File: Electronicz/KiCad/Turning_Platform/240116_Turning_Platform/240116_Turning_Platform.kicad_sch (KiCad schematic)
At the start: 5 parts, among them J1 Display, J2 +12V, J3 GND, J4 Conn_01x05_Pin

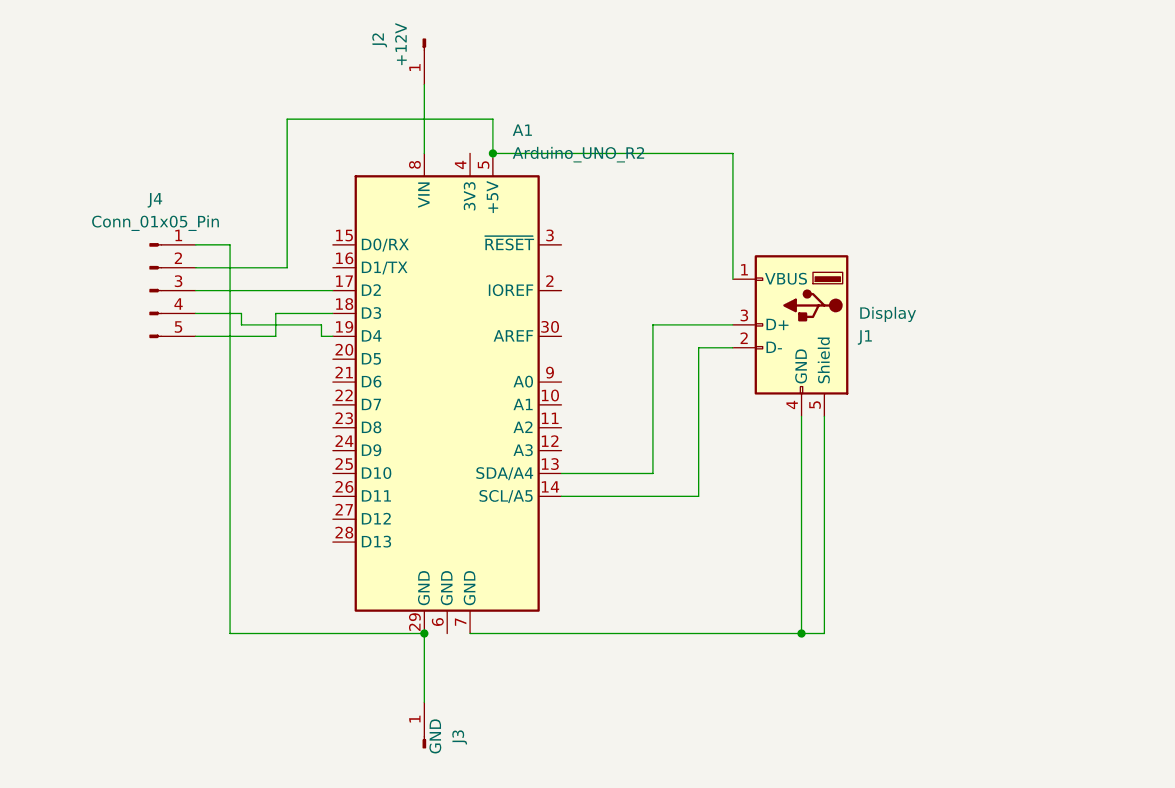
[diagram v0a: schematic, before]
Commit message: Make Turning Plate PCB
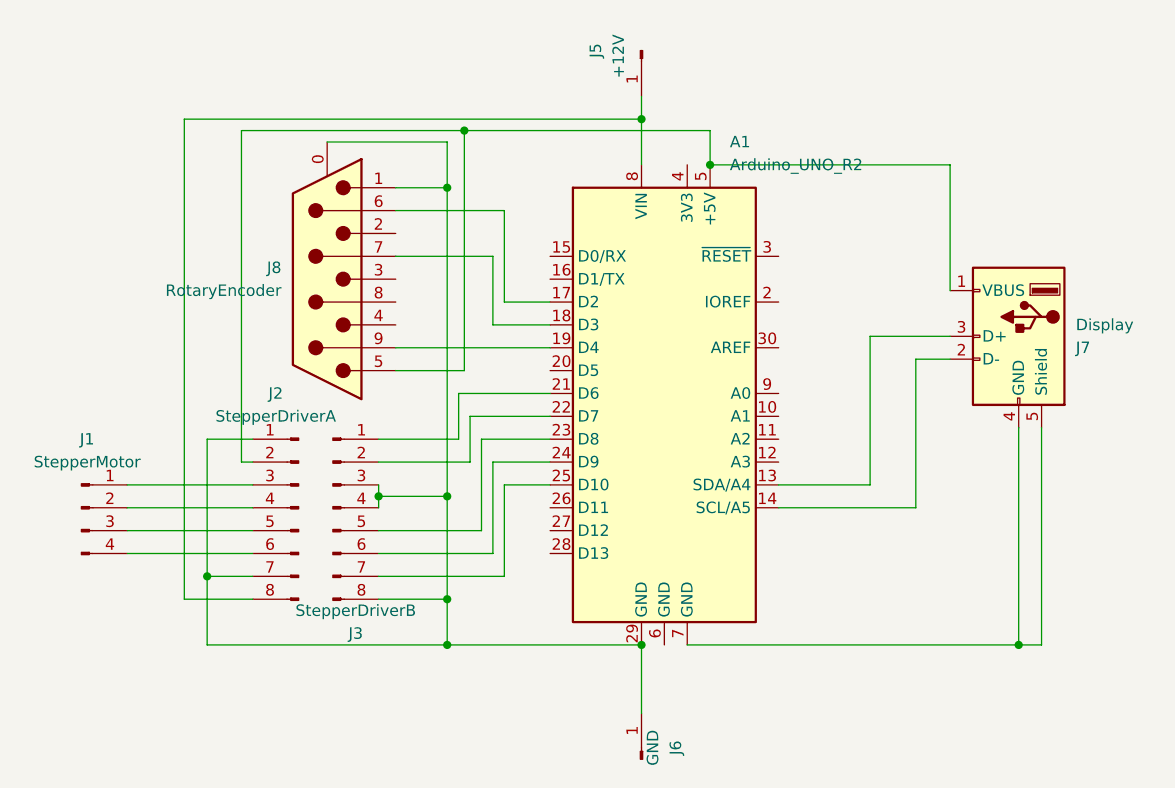
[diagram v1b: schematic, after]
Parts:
- removed J1: Display, Connector_USB:USB_A_CONNFLY_DS1095-WNR0, symbol Connector:USB_A
- removed J2: +12V, symbol Connector:Conn_01x01_Pin
- removed J3: GND, symbol Connector:Conn_01x01_Pin
- removed J4: Conn_01x05_Pin, symbol Connector:Conn_01x05_Pin
- added J1: StepperMotor, Connector_PinHeader_2.54mm:PinHeader_1x04_P2.54mm_Vertical, symbol Connector:Conn_01x04_Pin
- added J2: StepperDriverA, Connector_PinHeader_2.54mm:PinHeader_1x08_P2.54mm_Vertical, symbol Connector:Conn_01x08_Pin
- added J3: StepperDriverB, Connector_PinHeader_2.54mm:PinHeader_1x08_P2.54mm_Vertical, symbol Connector:Conn_01x08_Pin
- added J5: +12V, Connector_PinHeader_2.54mm:PinHeader_1x01_P2.54mm_Vertical, symbol Connector:Conn_01x01_Pin
- added J6: GND, Connector_PinHeader_2.54mm:PinHeader_1x01_P2.54mm_Vertical, symbol Connector:Conn_01x01_Pin
- added J7: Display, Connector_USB:USB_A_CONNFLY_DS1095-WNR0, symbol Connector:USB_A
- added J8: RotaryEncoder, Connector_Dsub:DSUB-9_Female_Horizontal_P2.77x2.84mm_EdgePinOffset7.70mm_Housed_MountingHolesOffset9.12mm, symbol Connector:DE9_Plug_MountingHoles
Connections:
- net at A1.5 (+5V): now also J2.2 (Pin_2), J7.1 (VBUS), J8.5
- net at A1.14 (SCL/A5): now also J7.2 (D-)
- net at A1.13 (SDA/A4): now also J7.3 (D+)
- net at A1.7 (GND): now also J7.4 (GND), J7.5 (Shield)
- net at A1.17 (D2): now also J8.6
- net at A1.18 (D3): now also J8.7
- net at A1.19 (D4): now also J8.9
- net at A1.21 (D6): now also J3.1 (Pin_1)
- net at A1.22 (D7): now also J3.2 (Pin_2)
- net at A1.23 (D8): now also J3.5 (Pin_5)
- net at A1.24 (D9): now also J3.6 (Pin_6)
- net at A1.25 (D10): now also J3.7 (Pin_7)
- net at A1.29 (GND): now also J2.1 (Pin_1), J2.7 (Pin_7), J3.3 (Pin_3), J3.4 (Pin_4), J3.8 (Pin_8), J6.1 (Pin_1), J8.0 (PAD), J8.1
- net at A1.8 (VIN): now also J2.8 (Pin_8), J5.1 (Pin_1)
- new net: J1.1 (Pin_1), J2.3 (Pin_3)
- new net: J1.2 (Pin_2), J2.4 (Pin_4)
- new net: J1.3 (Pin_3), J2.5 (Pin_5)
- new net: J1.4 (Pin_4), J2.6 (Pin_6)

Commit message: Update Turning Platform PCB
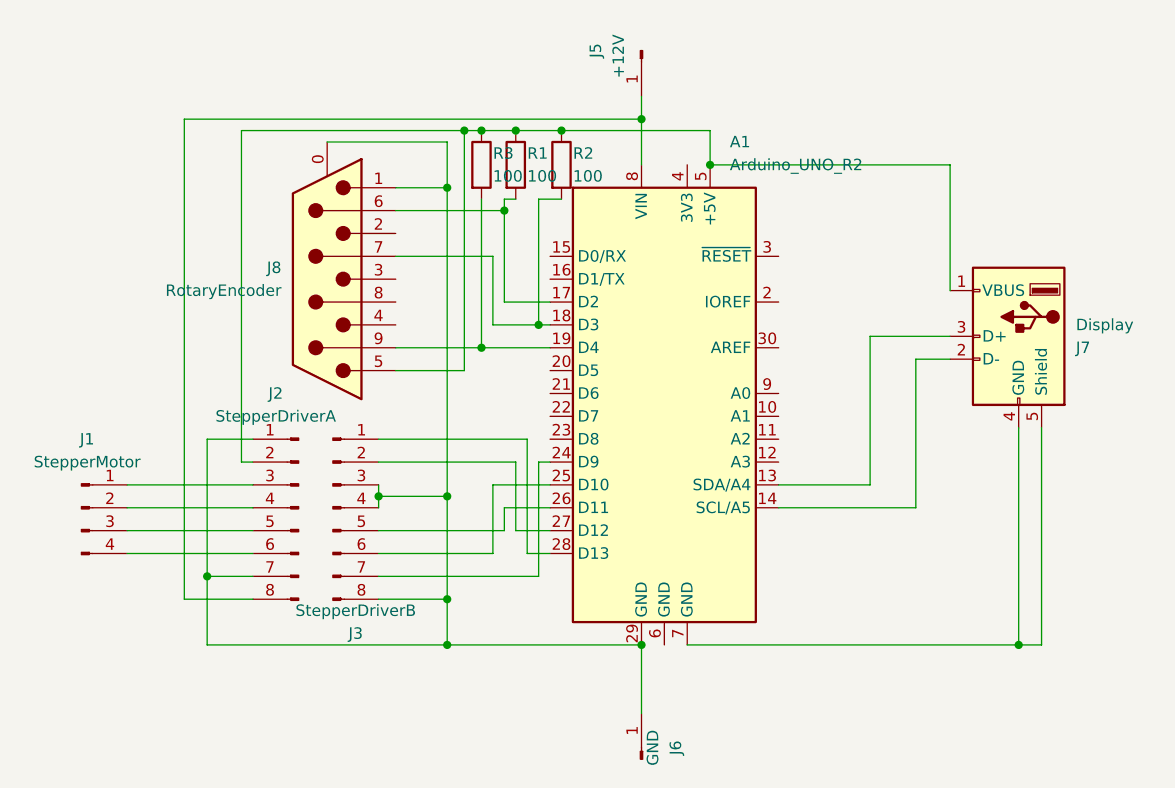
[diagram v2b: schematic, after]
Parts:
- added R1, R2, R3: 100, Resistor_THT:R_Axial_DIN0207_L6.3mm_D2.5mm_P10.16mm_Horizontal, symbol Device:R
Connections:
- net at A1.5 (+5V), J2.2 (Pin_2), J7.1 (VBUS)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: now also R1.1, R2.1, R3.1
- net at A1.17 (D2), J8.6: now also R1.2
- net at A1.18 (D3), J8.7: now also R2.2
- net at A1.19 (D4), J8.9: now also R3.2
- net at J3.1 (Pin_1): now also A1.28 (D13); no longer A1.21 (D6)
- net at J3.2 (Pin_2): now also A1.27 (D12); no longer A1.22 (D7)
- net at J3.5 (Pin_5): now also A1.26 (D11); no longer A1.23 (D8)
- net at J3.6 (Pin_6): now also A1.25 (D10); no longer A1.24 (D9)
- net at J3.7 (Pin_7): now also A1.24 (D9); no longer A1.25 (D10)

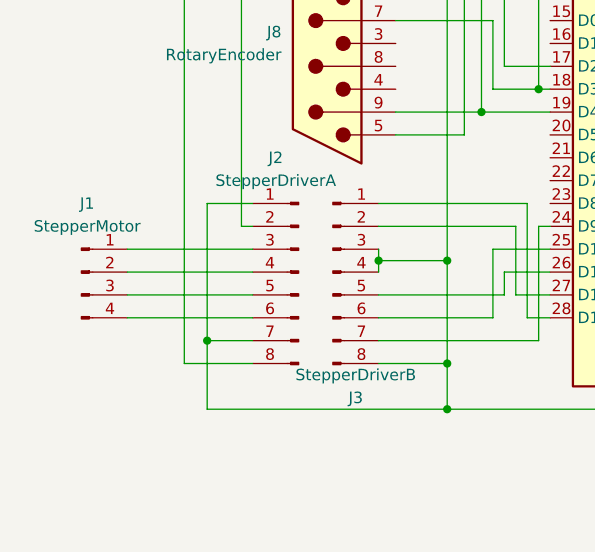
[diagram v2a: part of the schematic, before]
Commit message: Update Stepper Motor Connections
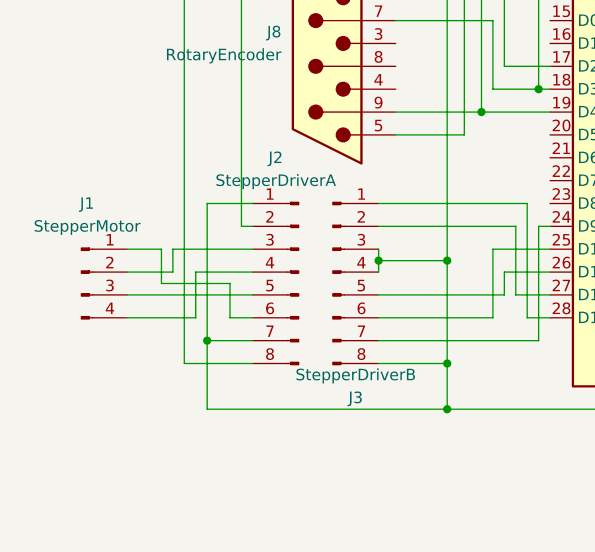
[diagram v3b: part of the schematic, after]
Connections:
- net at J2.3 (Pin_3): now also J1.2 (Pin_2); no longer J1.1 (Pin_1)
- net at J2.4 (Pin_4): now also J1.4 (Pin_4); no longer J1.2 (Pin_2)
- net at J2.6 (Pin_6): now also J1.1 (Pin_1); no longer J1.4 (Pin_4)
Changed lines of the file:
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@@
   (junction (at 129.54 53.34) (diameter 0) (color 0 0 0 0)
   )
+  (wire (pts (xy 101.6 86.36) (xy 95.25 86.36))
+    (stroke (width 0) (type default))
+  )
+  (wire (pts (xy 101.6 83.82) (xy 92.71 83.82))
+    (stroke (width 0) (type default))
+  )
   (wire (pts (xy 128.27 66.04) (xy 128.27 58.42))
     (stroke (width 0) (type default))
@@
     (stroke (width 0) (type default))
   )
+  (wire (pts (xy 91.44 83.82) (xy 91.44 87.63))
+    (stroke (width 0) (type default))
+  )
+  (wire (pts (xy 95.25 86.36) (xy 95.25 91.44))
+    (stroke (width 0) (type default))
+  )
   (wire (pts (xy 135.89 52.07) (xy 133.35 52.07))
     (stroke (width 0) (type default))
@@
     (stroke (width 0) (type default))
   )
+  (wire (pts (xy 87.63 83.82) (xy 91.44 83.82))
+    (stroke (width 0) (type default))
+  )
   (wire (pts (xy 134.62 66.04) (xy 133.35 66.04))
     (stroke (width 0) (type default))
@@
     (stroke (width 0) (type default))
   )
+  (wire (pts (xy 91.44 87.63) (xy 99.06 87.63))
+    (stroke (width 0) (type default))
+  )
   (wire (pts (xy 144.78 43.18) (xy 144.78 48.26))
     (stroke (width 0) (type default))
@@
     (stroke (width 0) (type default))
   )
+  (wire (pts (xy 95.25 91.44) (xy 87.63 91.44))
+    (stroke (width 0) (type default))
+  )
+  (wire (pts (xy 101.6 96.52) (xy 93.98 96.52))
+    (stroke (width 0) (type default))
+  )
+  (wire (pts (xy 170.18 67.31) (xy 179.07 67.31))
+    (stroke (width 0) (type default))
+  )
+  (wire (pts (xy 133.35 66.04) (xy 128.27 66.04))
+    (stroke (width 0) (type default))
+  )
+  (wire (pts (xy 175.26 86.36) (xy 175.26 69.85))
+    (stroke (width 0) (type default))
+  )
+  (wire (pts (xy 135.89 44.45) (xy 152.4 44.45))
+    (stroke (width 0) (type default))
+  )
+  (wire (pts (xy 130.81 81.28) (xy 130.81 88.9))
+    (stroke (width 0) (type default))
+  )
+  (wire (pts (xy 130.81 44.45) (xy 135.89 44.45))
+    (stroke (width 0) (type default))
+  )
+  (wire (pts (xy 129.54 52.07) (xy 129.54 53.34))
+    (stroke (width 0) (type default))
+  )
+  (wire (pts (xy 144.78 40.64) (xy 144.78 43.18))
+    (stroke (width 0) (type default))
+  )
+  (wire (pts (xy 101.6 78.74) (xy 96.52 78.74))
+    (stroke (width 0) (type default))
+  )
+  (wire (pts (xy 170.18 83.82) (xy 170.18 67.31))
+    (stroke (width 0) (type default))
+  )
+  (wire (pts (xy 115.57 83.82) (xy 115.57 85.09))
+    (stroke (width 0) (type default))
+  )
+  (wire (pts (xy 129.54 86.36) (xy 134.62 86.36))
+    (stroke (width 0) (type default))
+  )
+  (wire (pts (xy 101.6 81.28) (xy 100.33 81.28))
+    (stroke (width 0) (type default))
+  )
+  (wire (pts (xy 123.19 96.52) (xy 123.19 101.6))
+    (stroke (width 0) (type default))
+  )
+  (wire (pts (xy 117.475 68.58) (xy 127 68.58))
+    (stroke (width 0) (type default))
+  )
+  (wire (pts (xy 127 52.07) (xy 127 68.58))
+    (stroke (width 0) (type default))
+  )
+  (wire (pts (xy 130.81 88.9) (xy 134.62 88.9))
+    (stroke (width 0) (type default))
+  )
+  (wire (pts (xy 129.54 53.34) (xy 129.54 63.5))
+    (stroke (width 0) (type default))
+  )
+  (wire (pts (xy 92.71 86.36) (xy 87.63 86.36))
+    (stroke (width 0) (type default))
+  )
+  (wire (pts (xy 123.19 45.72) (xy 109.855 45.72))
+    (stroke (width 0) (type default))
+  )
+  (wire (pts (xy 128.27 83.82) (xy 134.62 83.82))
+    (stroke (width 0) (type default))
+  )
+  (wire (pts (xy 152.4 48.26) (xy 179.07 48.26))
+    (stroke (width 0) (type default))
+  )
+  (wire (pts (xy 99.06 91.44) (xy 101.6 91.44))
+    (stroke (width 0) (type default))
+  )
+  (wire (pts (xy 92.71 83.82) (xy 92.71 86.36))
+    (stroke (width 0) (type default))
+  )
+  (wire (pts (xy 186.69 101.6) (xy 149.86 101.6))
+    (stroke (width 0) (type default))
+  )
+  (wire (pts (xy 100.33 44.45) (xy 125.095 44.45))
+    (stroke (width 0) (type default))
+  )
+  (wire (pts (xy 160.02 83.82) (xy 170.18 83.82))
+    (stroke (width 0) (type default))
+  )
+  (wire (pts (xy 133.35 93.98) (xy 133.35 81.28))
+    (stroke (width 0) (type default))
+  )
+  (wire (pts (xy 132.08 91.44) (xy 134.62 91.44))
+    (stroke (width 0) (type default))
+  )
+  (wire (pts (xy 99.06 87.63) (xy 99.06 91.44))
+    (stroke (width 0) (type default))
+  )
+  (wire (pts (xy 175.26 69.85) (xy 179.07 69.85))
+    (stroke (width 0) (type default))
+  )
+  (wire (pts (xy 93.98 43.18) (xy 144.78 43.18))
+    (stroke (width 0) (type default))
+  )
+  (wire (pts (xy 96.52 101.6) (xy 123.19 101.6))
+    (stroke (width 0) (type default))
+  )
+  (wire (pts (xy 117.475 71.12) (xy 125.095 71.12))
+    (stroke (width 0) (type default))
+  )
+  (wire (pts (xy 117.475 50.8) (xy 123.19 50.8))
+    (stroke (width 0) (type default))
+  )
+  (wire (pts (xy 115.57 81.28) (xy 130.81 81.28))
+    (stroke (width 0) (type default))
+  )
+  (wire (pts (xy 115.57 91.44) (xy 128.27 91.44))
+    (stroke (width 0) (type default))
+  )
+  (wire (pts (xy 96.52 93.98) (xy 101.6 93.98))
+    (stroke (width 0) (type default))
+  )
+  (wire (pts (xy 186.69 77.47) (xy 186.69 101.6))
+    (stroke (width 0) (type default))
+  )
+  (wire (pts (xy 115.57 78.74) (xy 132.08 78.74))
+    (stroke (width 0) (type default))
+  )
+  (wire (pts (xy 133.35 81.28) (xy 134.62 81.28))
+    (stroke (width 0) (type default))
+  )
   (wire (pts (xy 87.63 88.9) (xy 101.6 88.9))
     (stroke (width 0) (type default))
   )
-  (wire (pts (xy 101.6 96.52) (xy 93.98 96.52))
-    (stroke (width 0) (type default))
-  )
-  (wire (pts (xy 170.18 67.31) (xy 179.07 67.31))
-    (stroke (width 0) (type default))
-  )
-  (wire (pts (xy 133.35 66.04) (xy 128.27 66.04))
-    (stroke (width 0) (type default))
-  )
-  (wire (pts (xy 87.63 86.36) (xy 101.6 86.36))
-    (stroke (width 0) (type default))
-  )
-  (wire (pts (xy 175.26 86.36) (xy 175.26 69.85))
-    (stroke (width 0) (type default))
-  )
-  (wire (pts (xy 135.89 44.45) (xy 152.4 44.45))
-    (stroke (width 0) (type default))
-  )
-  (wire (pts (xy 130.81 81.28) (xy 130.81 88.9))
-    (stroke (width 0) (type default))
-  )
-  (wire (pts (xy 130.81 44.45) (xy 135.89 44.45))
-    (stroke (width 0) (type default))
-  )
-  (wire (pts (xy 129.54 52.07) (xy 129.54 53.34))
-    (stroke (width 0) (type default))
-  )
-  (wire (pts (xy 144.78 40.64) (xy 144.78 43.18))
-    (stroke (width 0) (type default))
-  )
-  (wire (pts (xy 101.6 78.74) (xy 96.52 78.74))
-    (stroke (width 0) (type default))
-  )
-  (wire (pts (xy 170.18 83.82) (xy 170.18 67.31))
-    (stroke (width 0) (type default))
-  )
-  (wire (pts (xy 115.57 83.82) (xy 115.57 85.09))
-    (stroke (width 0) (type default))
-  )
-  (wire (pts (xy 129.54 86.36) (xy 134.62 86.36))
-    (stroke (width 0) (type default))
-  )
-  (wire (pts (xy 101.6 81.28) (xy 100.33 81.28))
-    (stroke (width 0) (type default))
-  )
-  (wire (pts (xy 123.19 96.52) (xy 123.19 101.6))
-    (stroke (width 0) (type default))
-  )
-  (wire (pts (xy 117.475 68.58) (xy 127 68.58))
-    (stroke (width 0) (type default))
-  )
-  (wire (pts (xy 127 52.07) (xy 127 68.58))
-    (stroke (width 0) (type default))
-  )
-  (wire (pts (xy 130.81 88.9) (xy 134.62 88.9))
-    (stroke (width 0) (type default))
-  )
-  (wire (pts (xy 129.54 53.34) (xy 129.54 63.5))
-    (stroke (width 0) (type default))
-  )
-  (wire (pts (xy 123.19 45.72) (xy 109.855 45.72))
-    (stroke (width 0) (type default))
-  )
-  (wire (pts (xy 128.27 83.82) (xy 134.62 83.82))
-    (stroke (width 0) (type default))
-  )
-  (wire (pts (xy 152.4 48.26) (xy 179.07 48.26))
-    (stroke (width 0) (type default))
-  )
-  (wire (pts (xy 186.69 101.6) (xy 149.86 101.6))
-    (stroke (width 0) (type default))
-  )
-  (wire (pts (xy 100.33 44.45) (xy 125.095 44.45))
-    (stroke (width 0) (type default))
-  )
-  (wire (pts (xy 87.63 83.82) (xy 101.6 83.82))
-    (stroke (width 0) (type default))
-  )
-  (wire (pts (xy 160.02 83.82) (xy 170.18 83.82))
-    (stroke (width 0) (type default))
-  )
-  (wire (pts (xy 133.35 93.98) (xy 133.35 81.28))
-    (stroke (width 0) (type default))
-  )
-  (wire (pts (xy 132.08 91.44) (xy 134.62 91.44))
-    (stroke (width 0) (type default))
-  )
-  (wire (pts (xy 175.26 69.85) (xy 179.07 69.85))
-    (stroke (width 0) (type default))
-  )
-  (wire (pts (xy 93.98 43.18) (xy 144.78 43.18))
-    (stroke (width 0) (type default))
-  )
-  (wire (pts (xy 96.52 101.6) (xy 123.19 101.6))
-    (stroke (width 0) (type default))
-  )
-  (wire (pts (xy 117.475 71.12) (xy 125.095 71.12))
-    (stroke (width 0) (type default))
-  )
-  (wire (pts (xy 117.475 50.8) (xy 123.19 50.8))
-    (stroke (width 0) (type default))
-  )
-  (wire (pts (xy 115.57 81.28) (xy 130.81 81.28))
-    (stroke (width 0) (type default))
-  )
-  (wire (pts (xy 115.57 91.44) (xy 128.27 91.44))
-    (stroke (width 0) (type default))
-  )
-  (wire (pts (xy 96.52 93.98) (xy 101.6 93.98))
-    (stroke (width 0) (type default))
-  )
-  (wire (pts (xy 186.69 77.47) (xy 186.69 101.6))
-    (stroke (width 0) (type default))
-  )
-  (wire (pts (xy 87.63 91.44) (xy 101.6 91.44))
-    (stroke (width 0) (type default))
-  )
-  (wire (pts (xy 115.57 78.74) (xy 132.08 78.74))
-    (stroke (width 0) (type default))
-  )
-  (wire (pts (xy 133.35 81.28) (xy 134.62 81.28))
-    (stroke (width 0) (type default))
-  )

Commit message: Update Stepper Connections Again because they are not the same on both StepperMotors
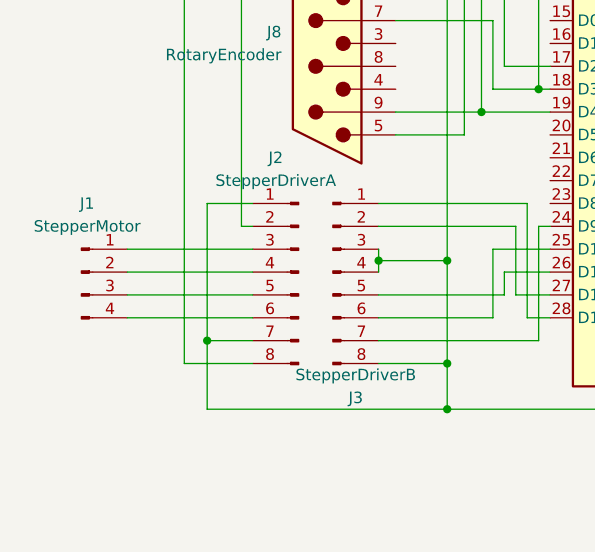
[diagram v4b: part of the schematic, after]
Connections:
- net at J2.3 (Pin_3): now also J1.1 (Pin_1); no longer J1.2 (Pin_2)
- net at J2.4 (Pin_4): now also J1.2 (Pin_2); no longer J1.4 (Pin_4)
- net at J2.6 (Pin_6): now also J1.4 (Pin_4); no longer J1.1 (Pin_1)
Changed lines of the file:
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@@
   (junction (at 129.54 53.34) (diameter 0) (color 0 0 0 0)
   )
-  (wire (pts (xy 101.6 86.36) (xy 95.25 86.36))
+  (wire (pts (xy 87.63 86.36) (xy 101.6 86.36))
     (stroke (width 0) (type default))
   )
-  (wire (pts (xy 101.6 83.82) (xy 92.71 83.82))
+  (wire (pts (xy 87.63 83.82) (xy 101.6 83.82))
     (stroke (width 0) (type default))
   )
@@
   )
   (wire (pts (xy 189.23 101.6) (xy 186.69 101.6))
-    (stroke (width 0) (type default))
-  )
-  (wire (pts (xy 91.44 83.82) (xy 91.44 87.63))
-    (stroke (width 0) (type default))
-  )
-  (wire (pts (xy 95.25 86.36) (xy 95.25 91.44))
     (stroke (width 0) (type default))
   )
@@
     (stroke (width 0) (type default))
   )
-  (wire (pts (xy 87.63 83.82) (xy 91.44 83.82))
-    (stroke (width 0) (type default))
-  )
   (wire (pts (xy 134.62 66.04) (xy 133.35 66.04))
     (stroke (width 0) (type default))
@@
   )
   (wire (pts (xy 125.095 44.45) (xy 125.095 71.12))
-    (stroke (width 0) (type default))
-  )
-  (wire (pts (xy 91.44 87.63) (xy 99.06 87.63))
     (stroke (width 0) (type default))
   )
@@
   )
   (wire (pts (xy 100.33 81.28) (xy 100.33 44.45))
-    (stroke (width 0) (type default))
-  )
-  (wire (pts (xy 95.25 91.44) (xy 87.63 91.44))
     (stroke (width 0) (type default))
   )
@@
     (stroke (width 0) (type default))
   )
-  (wire (pts (xy 92.71 86.36) (xy 87.63 86.36))
-    (stroke (width 0) (type default))
-  )
   (wire (pts (xy 123.19 45.72) (xy 109.855 45.72))
     (stroke (width 0) (type default))
@@
     (stroke (width 0) (type default))
   )
-  (wire (pts (xy 99.06 91.44) (xy 101.6 91.44))
-    (stroke (width 0) (type default))
-  )
-  (wire (pts (xy 92.71 83.82) (xy 92.71 86.36))
+  (wire (pts (xy 87.63 91.44) (xy 101.6 91.44))
     (stroke (width 0) (type default))
   )
@@
     (stroke (width 0) (type default))
   )
-  (wire (pts (xy 99.06 87.63) (xy 99.06 91.44))
-    (stroke (width 0) (type default))
-  )

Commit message: Plot Turning Platform PCB
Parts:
- added C1: C, Capacitor_THT:CP_Radial_D10.0mm_P7.50mm, symbol Device:C
- added R4: 100, Resistor_THT:R_Axial_DIN0207_L6.3mm_D2.5mm_P10.16mm_Horizontal, symbol Device:R
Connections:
- net at A1.29 (GND), J2.1 (Pin_1), J2.7 (Pin_7)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: now also C1.1; no longer J8.0 (PAD)
- net at J8.3: now also J8.7, R2.2, C1.2, R4.1
- new net: A1.18 (D3), R4.2
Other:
- moved on the sheet: J8
